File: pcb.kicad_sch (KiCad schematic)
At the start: 19 parts

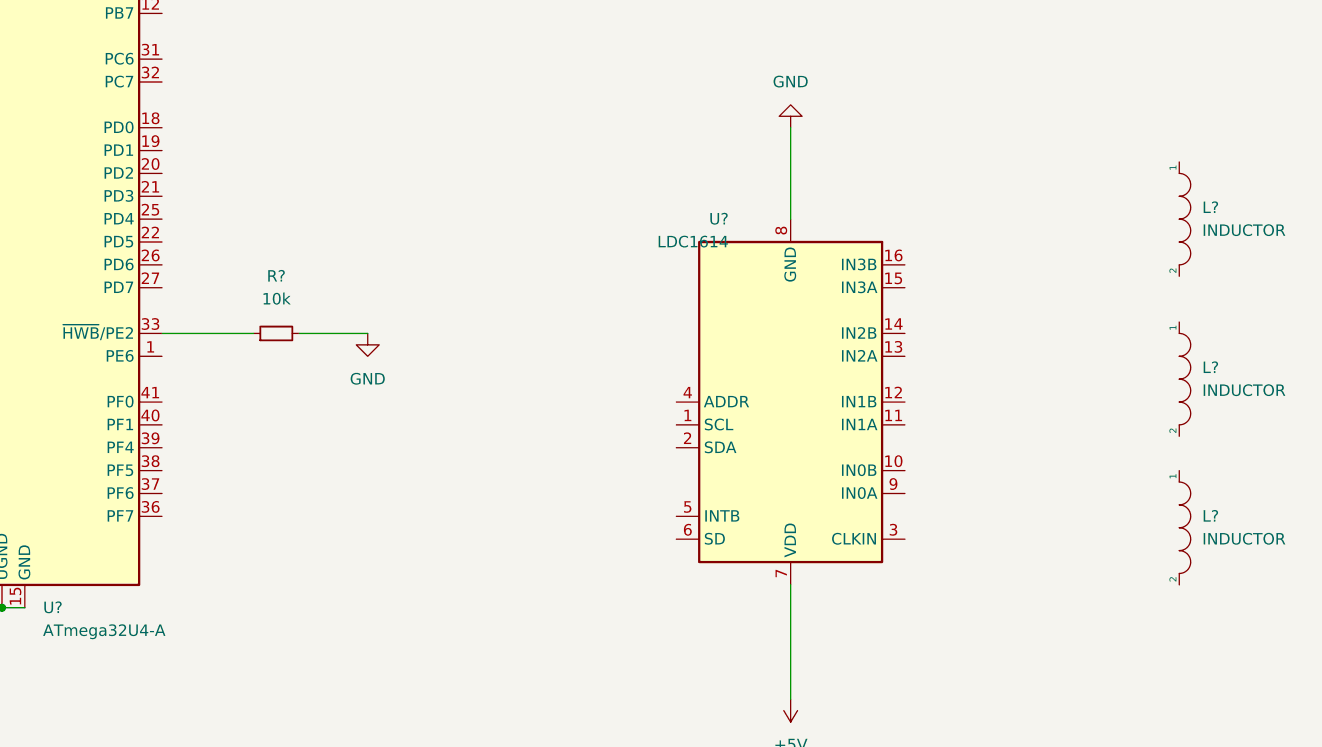
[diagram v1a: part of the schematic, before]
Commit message: usb c added
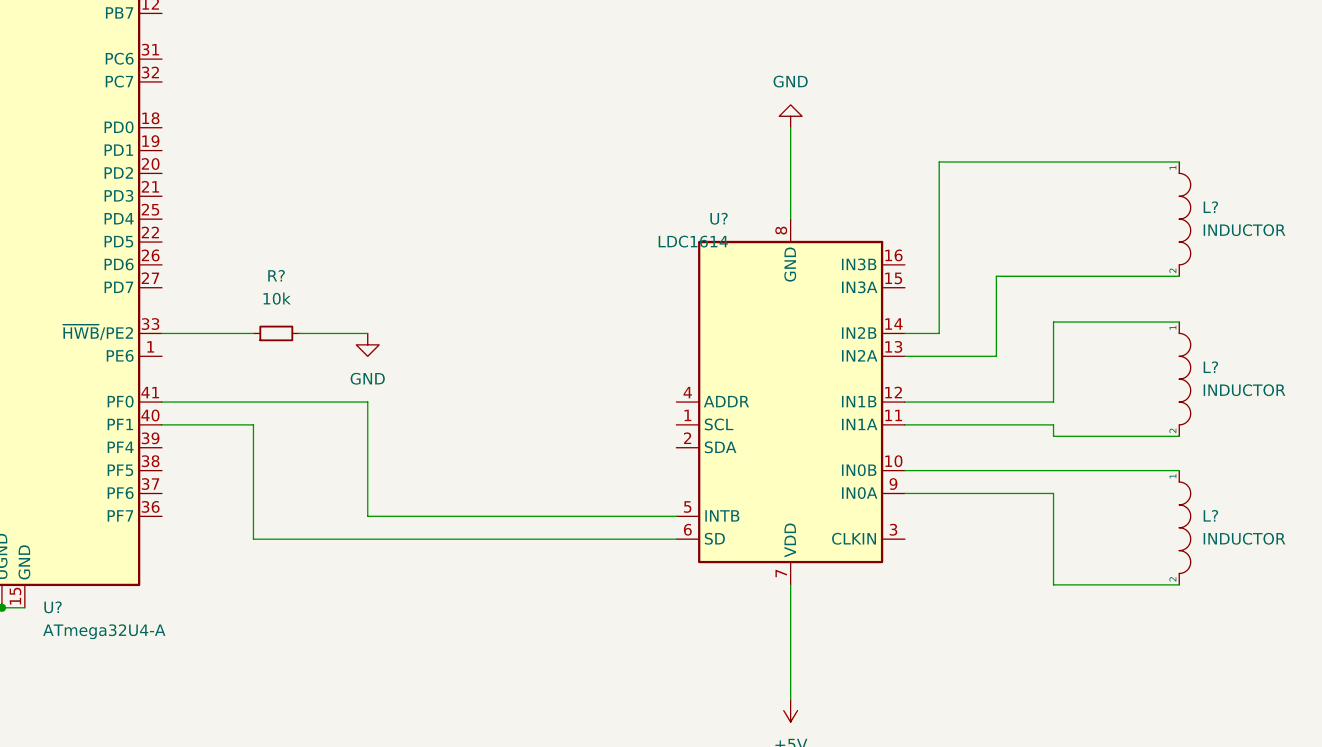
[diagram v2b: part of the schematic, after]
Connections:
- net at L?.1: now also U?.14 (IN2B)
- net at L?.2: now also U?.13 (IN2A)
- net at L?.1: now also U?.10 (IN0B)
- net at L?.2: now also U?.9 (IN0A)
- net at U?.11 (IN1A): now also L?.2
- net at U?.12 (IN1B): now also L?.1
- net at U?.5 (INTB): now also U?.41 (PF0)
- net at U?.6 (SD): now also U?.40 (PF1)
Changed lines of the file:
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@@
+    (stroke (width 0) (type default) (color 0 0 0 0))
+  )
+  (wire (pts (xy 177.8 119.38) (xy 177.8 106.68))
     (stroke (width 0) (type default) (color 0 0 0 0))
   )
@@
     (stroke (width 0) (type default) (color 0 0 0 0))
   )
+  (wire (pts (xy 237.49 116.84) (xy 254 116.84))
+    (stroke (width 0) (type default) (color 0 0 0 0))
+  )
   (wire (pts (xy 124.46 66.04) (xy 101.6 66.04))
     (stroke (width 0) (type default) (color 0 0 0 0))
@@
     (stroke (width 0) (type default) (color 0 0 0 0))
   )
+  (wire (pts (xy 165.1 109.22) (xy 165.1 121.92))
+    (stroke (width 0) (type default) (color 0 0 0 0))
+  )
+  (wire (pts (xy 241.3 99.06) (xy 241.3 80.01))
+    (stroke (width 0) (type default) (color 0 0 0 0))
+  )
+  (wire (pts (xy 247.65 92.71) (xy 247.65 101.6))
+    (stroke (width 0) (type default) (color 0 0 0 0))
+  )
+  (wire (pts (xy 165.1 121.92) (xy 212.09 121.92))
+    (stroke (width 0) (type default) (color 0 0 0 0))
+  )
   (wire (pts (xy 88.9 106.68) (xy 95.25 106.68))
     (stroke (width 0) (type default) (color 0 0 0 0))
   )
+  (wire (pts (xy 237.49 109.22) (xy 254 109.22))
+    (stroke (width 0) (type default) (color 0 0 0 0))
+  )
   (wire (pts (xy 101.6 106.68) (xy 114.3 106.68))
     (stroke (width 0) (type default) (color 0 0 0 0))
@@
     (stroke (width 0) (type default) (color 0 0 0 0))
   )
+  (wire (pts (xy 154.94 109.22) (xy 165.1 109.22))
+    (stroke (width 0) (type default) (color 0 0 0 0))
+  )
   (wire (pts (xy 93.98 50.8) (xy 101.6 50.8))
     (stroke (width 0) (type default) (color 0 0 0 0))
@@
     (stroke (width 0) (type default) (color 0 0 0 0))
   )
+  (wire (pts (xy 212.09 119.38) (xy 177.8 119.38))
+    (stroke (width 0) (type default) (color 0 0 0 0))
+  )
   (wire (pts (xy 101.6 50.8) (xy 124.46 50.8))
     (stroke (width 0) (type default) (color 0 0 0 0))
@@
     (stroke (width 0) (type default) (color 0 0 0 0))
   )
+  (wire (pts (xy 237.49 114.3) (xy 267.97 114.3))
+    (stroke (width 0) (type default) (color 0 0 0 0))
+  )
   (wire (pts (xy 88.9 58.42) (xy 88.9 63.5))
     (stroke (width 0) (type default) (color 0 0 0 0))
   )
+  (wire (pts (xy 154.94 106.68) (xy 177.8 106.68))
+    (stroke (width 0) (type default) (color 0 0 0 0))
+  )
+  (wire (pts (xy 254 106.68) (xy 254 97.79))
+    (stroke (width 0) (type default) (color 0 0 0 0))
+  )
   (wire (pts (xy 106.68 73.66) (xy 124.46 73.66))
     (stroke (width 0) (type default) (color 0 0 0 0))
@@
     (stroke (width 0) (type default) (color 0 0 0 0))
   )
+  (wire (pts (xy 237.49 101.6) (xy 247.65 101.6))
+    (stroke (width 0) (type default) (color 0 0 0 0))
+  )
   (wire (pts (xy 99.06 53.34) (xy 99.06 58.42))
     (stroke (width 0) (type default) (color 0 0 0 0))
@@
     (stroke (width 0) (type default) (color 0 0 0 0))
   )
+  (wire (pts (xy 267.97 92.71) (xy 247.65 92.71))
+    (stroke (width 0) (type default) (color 0 0 0 0))
+  )
   (wire (pts (xy 124.46 78.74) (xy 111.76 78.74))
     (stroke (width 0) (type default) (color 0 0 0 0))
@@
     (stroke (width 0) (type default) (color 0 0 0 0))
   )
+  (wire (pts (xy 237.49 99.06) (xy 241.3 99.06))
+    (stroke (width 0) (type default) (color 0 0 0 0))
+  )
   (wire (pts (xy 120.65 24.13) (xy 120.65 27.94))
     (stroke (width 0) (type default) (color 0 0 0 0))
@@
     (stroke (width 0) (type default) (color 0 0 0 0))
   )
+  (wire (pts (xy 241.3 80.01) (xy 267.97 80.01))
+    (stroke (width 0) (type default) (color 0 0 0 0))
+  )
   (wire (pts (xy 88.9 71.12) (xy 109.22 71.12))
     (stroke (width 0) (type default) (color 0 0 0 0))
@@
     (stroke (width 0) (type default) (color 0 0 0 0))
   )
+  (wire (pts (xy 237.49 106.68) (xy 254 106.68))
+    (stroke (width 0) (type default) (color 0 0 0 0))
+  )
+  (wire (pts (xy 254 127) (xy 254 116.84))
+    (stroke (width 0) (type default) (color 0 0 0 0))
+  )
   (wire (pts (xy 95.25 96.52) (xy 95.25 101.6))
     (stroke (width 0) (type default) (color 0 0 0 0))
   )
+  (wire (pts (xy 254 110.49) (xy 254 109.22))
+    (stroke (width 0) (type default) (color 0 0 0 0))
+  )
+  (wire (pts (xy 267.97 110.49) (xy 254 110.49))
+    (stroke (width 0) (type default) (color 0 0 0 0))
+  )
   (wire (pts (xy 111.76 83.82) (xy 111.76 88.9))
     (stroke (width 0) (type default) (color 0 0 0 0))
@@
     (stroke (width 0) (type default) (color 0 0 0 0))
   )
+  (wire (pts (xy 267.97 127) (xy 254 127))
+    (stroke (width 0) (type default) (color 0 0 0 0))
+  )
+  (wire (pts (xy 254 97.79) (xy 267.97 97.79))
+    (stroke (width 0) (type default) (color 0 0 0 0))
+  )

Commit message: usb c
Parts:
- removed J?: USB_C_Receptacle_USB2.0, symbol Connector:USB_C_Receptacle_USB2.0
- added F?: Polyfuse_Small, Fuse:Fuse_1206_3216Metric_Pad1.42x1.75mm_HandSolder, symbol Device:Polyfuse_Small
- added R? (x2): 5.1k, Resistor_SMD:R_0805_2012Metric_Pad1.15x1.40mm_HandSolder, symbol Device:R_Small
- added U?: PRTR5V0U2X, random-keyboard-parts:SOT143B, symbol random-keyboard-parts:PRTR5V0U2X
- added USB?: HRO-TYPE-C-31-M-12, Type-C:HRO-TYPE-C-31-M-12-HandSoldering, symbol Type-C:HRO-TYPE-C-31-M-12
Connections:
- net +5V: now also F?.1; no longer U?.7 (VDD)
- net D+: now also U?.2 (IO1), USB?.6 (DP1), USB?.8 (DP2)
- net D-: now also U?.3 (IO2), USB?.5 (DN2), USB?.7 (DN1)
- net GND: now also R?.1, R?.1, U?.1 (GND), USB?.1 (GND), USB?.12 (GND), USB?.13 (SHIELD); no longer U?.17 (GND), U?.8 (GND)
- net at L?.1: no longer U?.14 (IN2B)
- net at L?.2: no longer U?.13 (IN2A)
- net at L?.1: no longer U?.10 (IN0B)
- net at L?.2: no longer U?.9 (IN0A)
- net at U?.11 (IN1A): no longer L?.2
- net at U?.12 (IN1B): no longer L?.1
- net at U?.5 (INTB): no longer U?.41 (PF0)
- net at U?.6 (SD): no longer U?.40 (PF1)
- new net: U?.17 (GND), U?.8 (GND)
- new net: R?.2, USB?.10 (CC2)
- new net: R?.2, USB?.4 (CC1)
- new net VCC: F?.2, U?.4 (VCC), USB?.11 (VBUS), USB?.2 (VBUS)
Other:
- moved on the sheet: C?, L?, R?, SW?, U?, Y?

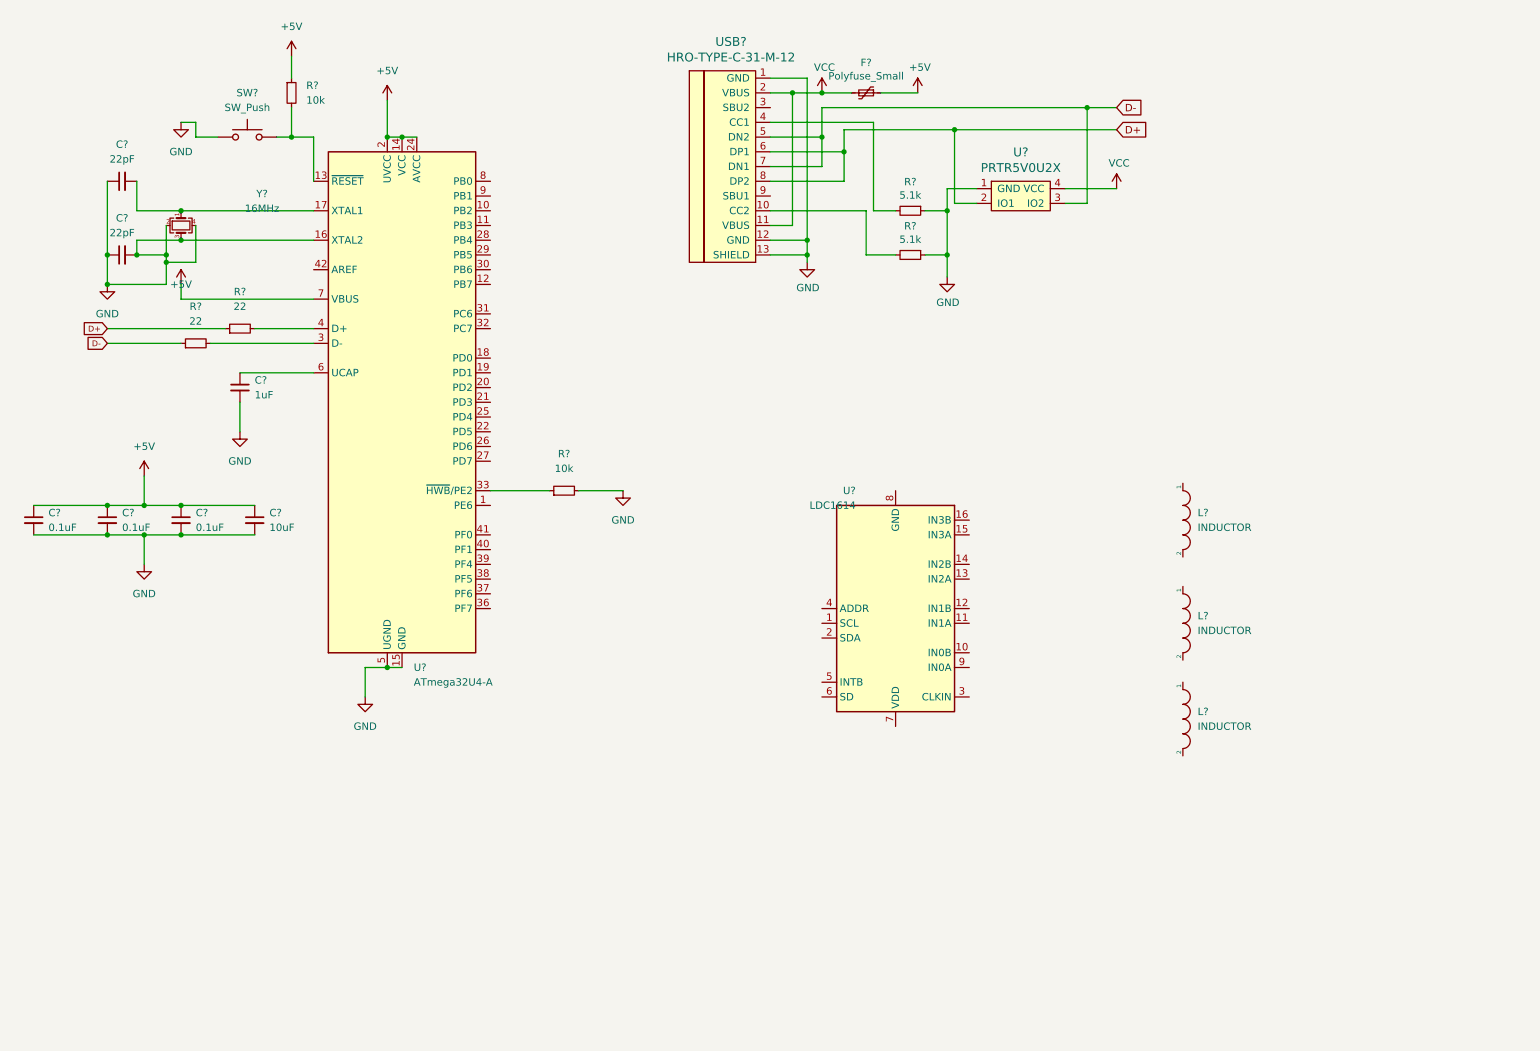
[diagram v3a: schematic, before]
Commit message: 3.3v conversion added
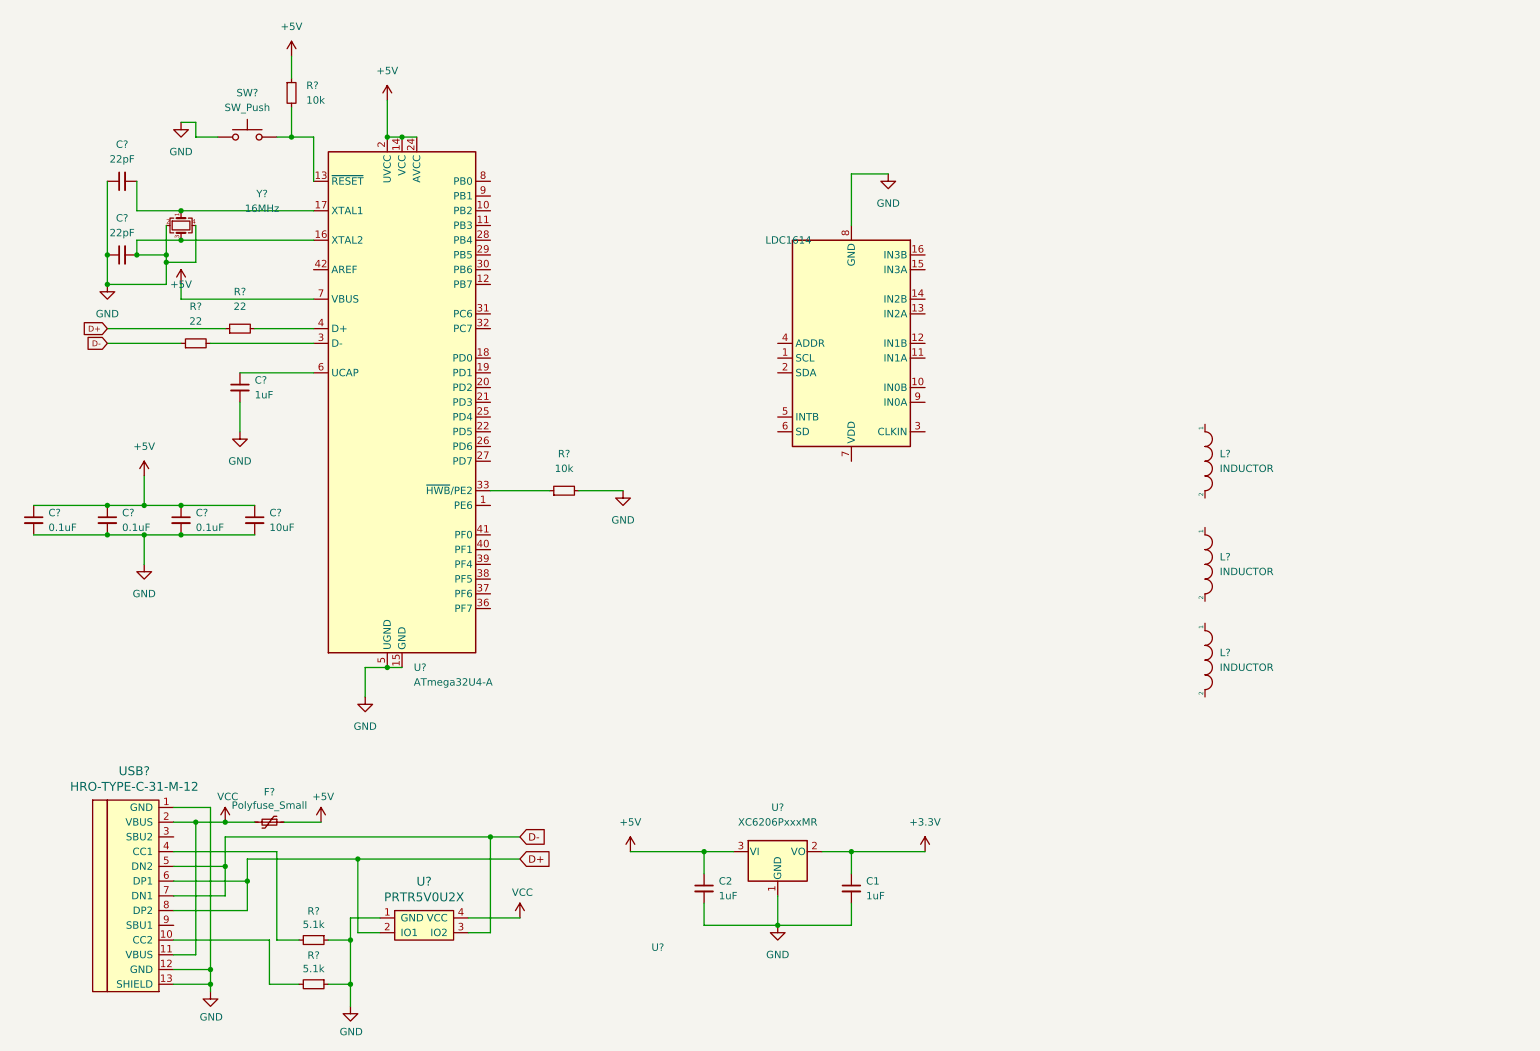
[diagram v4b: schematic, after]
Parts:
- added C1, C2: 1uF, symbol Device:C_Small
- added U?: XC6206PxxxMR, Package_TO_SOT_SMD:SOT-23-3, symbol Regulator_Linear:XC6206PxxxMR
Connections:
- net +5V: now also C2.1, U?.3 (VI)
- net GND: now also U?.17 (GND), U?.8 (GND), C1.2, C2.2, U?.1 (GND)
- new net +3.3V: C1.1, U?.2 (VO)
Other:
- moved on the sheet: F?, L?, R?, U?, USB?
